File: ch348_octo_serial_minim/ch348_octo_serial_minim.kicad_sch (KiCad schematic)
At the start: 41 parts, among them J1 USB_C_Receptacle_USB2.0, J10 JLCPCB_3.5MM_SOCKET_C18166, J12 JLCPCB_3.5MM_SOCKET_C18166, J14 JLCPCB_3.5MM_SOCKET_C18166, J16 JLCPCB_3.5MM_SOCKET_C18166, J18 JLCPCB_3.5MM_SOCKET_C18166, J2 Conn_01x01, J20 JLCPCB_3.5MM_SOCKET_C18166, J3 Conn_01x01, J4 Conn_01x01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

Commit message: ch348_octo_serial_minim: jan2023 rev ready for production
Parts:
- removed R1, R9: 1k, tom-passives:R_0402_1005Metric, symbol jlcpcb-basic-resistor-0402:1k
- added J22, J23: Conn_01x16, tom-connectors:PinHeader_1x16_P2.54mm_Horizontal, symbol tom-connectors:Conn_01x16
- added R1: 2.4k, R_0402_1005Metric, symbol jlcpcb-basic-resistor-0402:2.4k
- added R9: 1.5k, R_0402_1005Metric, symbol jlcpcb-basic-resistor-0402:1.5k
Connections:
- net +3.3V: now also J22.10 (Pin_10), J22.14 (Pin_14), J22.2 (Pin_2), J22.6 (Pin_6), J23.10 (Pin_10), J23.14 (Pin_14), J23.2 (Pin_2), J23.6 (Pin_6), R1.1
- net GND: now also J22.1 (Pin_1), J22.13 (Pin_13), J22.5 (Pin_5), J22.9 (Pin_9), J23.1 (Pin_1), J23.13 (Pin_13), J23.5 (Pin_5), J23.9 (Pin_9)
- net RXD0: now also J22.4 (Pin_4)
- net RXD1: now also J22.8 (Pin_8)
- net RXD2: now also J22.12 (Pin_12)
- net RXD3: now also J22.16 (Pin_16)
- net RXD4: now also J23.4 (Pin_4)
- net RXD5: now also J23.8 (Pin_8)
- net RXD6: now also J23.12 (Pin_12)
- net RXD7: now also J23.16 (Pin_16)
- net TXD0: now also J22.3 (Pin_3)
- net TXD1: now also J22.7 (Pin_7)
- net TXD2: now also J22.11 (Pin_11)
- net TXD3: now also J22.15 (Pin_15)
- net TXD4: now also J23.3 (Pin_3)
- net TXD5: now also J23.7 (Pin_7)
- net TXD6: now also J23.11 (Pin_11)
- net TXD7: now also J23.15 (Pin_15)
- net TX_S: now also R9.2
- net at D4.2 (A): now also R9.1
- net at D1.2 (A): now also R1.2
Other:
- sheet Serial Connector 0 ports: added none; removed CTS, DTR, RTS, RXD, TXD
- sheet Serial Connector 1 ports: added none; removed CTS, DTR, RTS, RXD, TXD
- sheet Serial Connector 2 ports: added none; removed CTS, DTR, RTS, RXD, TXD
- sheet Serial Connector 3 ports: added none; removed CTS, DTR, RTS, RXD, TXD
- sheet Serial Connector 4 ports: added none; removed CTS, DTR, RTS, RXD, TXD
- sheet Serial Connector 5 ports: added none; removed CTS, DTR, RTS, RXD, TXD
- sheet Serial Connector 6 ports: added none; removed CTS, DTR, RTS, RXD, TXD
- sheet Serial Connector 7 ports: added none; removed CTS, DTR, RTS, RXD, TXD
- note removed: "Update led resistors!"
- note removed: "horizontal with most stock C725908"
- moved on the sheet: C11, C7, C9

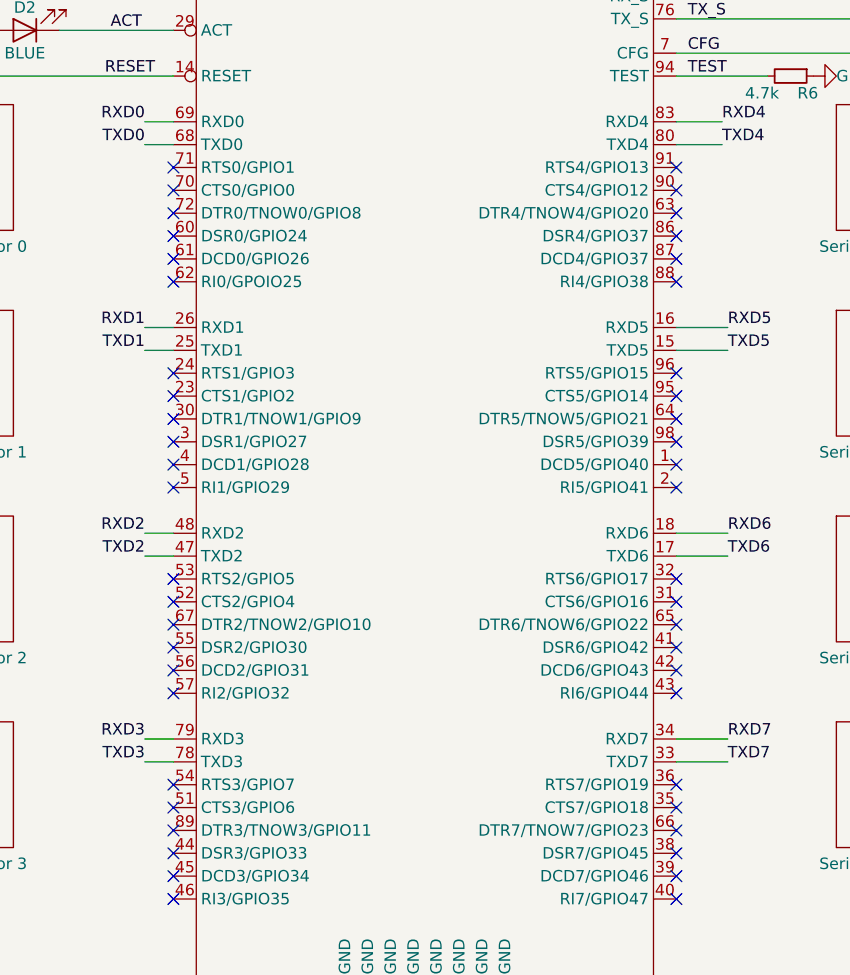
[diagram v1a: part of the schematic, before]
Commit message: ch348_octo_serial_minim: move plate to subdir, add cts/rts link, Jan2023a
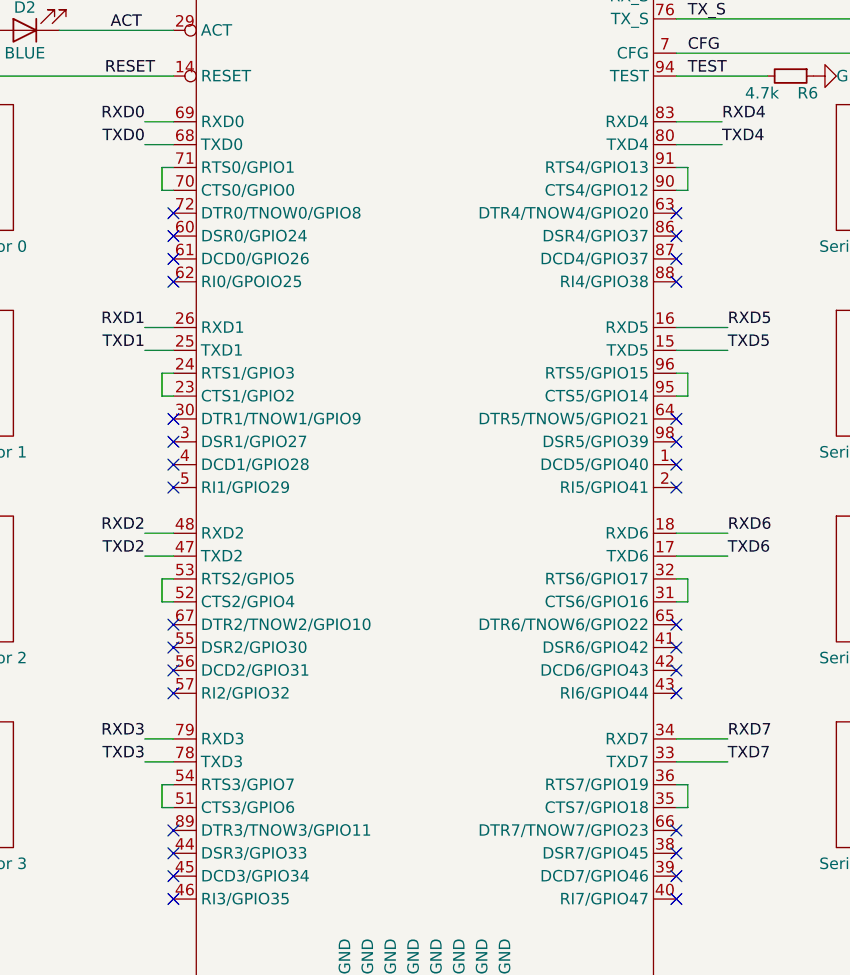
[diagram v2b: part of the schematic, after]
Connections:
- net at U1.23 (CTS1/GPIO2): now also U1.24 (RTS1/GPIO3)
- net at U1.31 (CTS6/GPIO16): now also U1.32 (RTS6/GPIO17)
- net at U1.35 (CTS7/GPIO18): now also U1.36 (RTS7/GPIO19)
- net at U1.51 (CTS3/GPIO6): now also U1.54 (RTS3/GPIO7)
- net at U1.52 (CTS2/GPIO4): now also U1.53 (RTS2/GPIO5)
- net at U1.70 (CTS0/GPIO0): now also U1.71 (RTS0/GPIO1)
- net at U1.90 (CTS4/GPIO12): now also U1.91 (RTS4/GPIO13)
- net at U1.95 (CTS5/GPIO14): now also U1.96 (RTS5/GPIO15)
- no-connect marks 54 -> 38
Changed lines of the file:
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@@
   (junction (at 58.42 81.915) (diameter 0) (color 0 0 0 0)
   )
-  (no_connect (at 165.735 83.82))
   (no_connect (at 109.855 132.08))
   (no_connect (at 109.855 71.12))
@@
   (no_connect (at 109.855 109.22))
   (no_connect (at 40.64 48.26))
-  (no_connect (at 109.855 58.42))
   (no_connect (at 165.735 137.16))
-  (no_connect (at 109.855 106.68))
   (no_connect (at 109.855 86.36))
   (no_connect (at 40.64 50.8))
-  (no_connect (at 165.735 104.14))
-  (no_connect (at 109.855 81.28))
-  (no_connect (at 109.855 60.96))
-  (no_connect (at 165.735 81.28))
   (no_connect (at 165.735 114.3))
   (no_connect (at 109.855 88.9))
   (no_connect (at 165.735 88.9))
-  (no_connect (at 165.735 129.54))
-  (no_connect (at 165.735 127))
-  (no_connect (at 165.735 106.68))
   (no_connect (at 165.735 71.12))
   (no_connect (at 182.88 172.085))
@@
   (no_connect (at 165.735 68.58))
   (no_connect (at 165.735 66.04))
-  (no_connect (at 109.855 127))
   (no_connect (at 109.855 63.5))
   (no_connect (at 165.735 111.76))
-  (no_connect (at 109.855 129.54))
   (no_connect (at 165.735 139.7))
   (no_connect (at 207.01 172.085))
   (no_connect (at 109.855 116.84))
-  (no_connect (at 109.855 104.14))
   (no_connect (at 109.855 114.3))
   (no_connect (at 109.855 91.44))
-  (no_connect (at 165.735 58.42))
-  (no_connect (at 165.735 60.96))
-  (no_connect (at 109.855 83.82))
   (wire (pts (xy 165.735 48.26) (xy 175.895 48.26))
     (stroke (width 0) (type default) (color 0 0 0 0))
@@
     (stroke (width 0) (type default) (color 0 0 0 0))
   )
+  (wire (pts (xy 108.585 60.96) (xy 109.855 60.96))
+    (stroke (width 0) (type default) (color 0 0 0 0))
+  )
   (wire (pts (xy 62.23 176.53) (xy 62.23 179.705))
     (stroke (width 0) (type default) (color 0 0 0 0))
@@
     (stroke (width 0) (type default) (color 0 0 0 0))
   )
+  (wire (pts (xy 108.585 104.14) (xy 108.585 106.68))
+    (stroke (width 0) (type default) (color 0 0 0 0))
+  )
   (wire (pts (xy 66.04 43.815) (xy 76.2 43.815))
     (stroke (width 0) (type default) (color 0 0 0 0))
@@
     (stroke (width 0) (type default) (color 0 0 0 0))
   )
+  (wire (pts (xy 165.735 58.42) (xy 167.005 58.42))
+    (stroke (width 0) (type default) (color 0 0 0 0))
+  )
+  (wire (pts (xy 109.855 127) (xy 108.585 127))
+    (stroke (width 0) (type default) (color 0 0 0 0))
+  )
   (wire (pts (xy 90.805 176.53) (xy 90.805 179.705))
     (stroke (width 0) (type default) (color 0 0 0 0))
@@
     (stroke (width 0) (type default) (color 0 0 0 0))
   )
+  (wire (pts (xy 165.735 127) (xy 167.005 127))
+    (stroke (width 0) (type default) (color 0 0 0 0))
+  )
   (wire (pts (xy 40.64 178.435) (xy 31.115 178.435))
     (stroke (width 0) (type default) (color 0 0 0 0))
@@
     (stroke (width 0) (type default) (color 0 0 0 0))
   )
+  (wire (pts (xy 108.585 106.68) (xy 109.855 106.68))
+    (stroke (width 0) (type default) (color 0 0 0 0))
+  )
   (wire (pts (xy 41.91 33.02) (xy 41.91 35.56))
     (stroke (width 0) (type default) (color 0 0 0 0))
@@
     (stroke (width 0) (type default) (color 0 0 0 0))
   )
+  (wire (pts (xy 109.855 81.28) (xy 108.585 81.28))
+    (stroke (width 0) (type default) (color 0 0 0 0))
+  )
   (wire (pts (xy 97.155 43.18) (xy 109.855 43.18))
     (stroke (width 0) (type default) (color 0 0 0 0))
@@
     (stroke (width 0) (type default) (color 0 0 0 0))
   )
+  (wire (pts (xy 167.005 104.14) (xy 167.005 106.68))
+    (stroke (width 0) (type default) (color 0 0 0 0))
+  )
   (wire (pts (xy 26.67 176.53) (xy 26.67 179.705))
     (stroke (width 0) (type default) (color 0 0 0 0))
@@
     (stroke (width 0) (type default) (color 0 0 0 0))
   )
+  (wire (pts (xy 165.735 106.68) (xy 167.005 106.68))
+    (stroke (width 0) (type default) (color 0 0 0 0))
+  )
   (wire (pts (xy 45.72 176.53) (xy 45.72 179.705))
     (stroke (width 0) (type default) (color 0 0 0 0))
@@
     (stroke (width 0) (type default) (color 0 0 0 0))
   )
+  (wire (pts (xy 108.585 83.82) (xy 109.855 83.82))
+    (stroke (width 0) (type default) (color 0 0 0 0))
+  )
   (wire (pts (xy 253.365 130.81) (xy 258.445 130.81))
     (stroke (width 0) (type default) (color 0 0 0 0))
@@
     (stroke (width 0) (type default) (color 0 0 0 0))
   )
+  (wire (pts (xy 165.735 129.54) (xy 167.005 129.54))
+    (stroke (width 0) (type default) (color 0 0 0 0))
+  )
   (wire (pts (xy 79.375 121.92) (xy 78.105 121.92))
     (stroke (width 0) (type default) (color 0 0 0 0))
@@
     (stroke (width 0) (type default) (color 0 0 0 0))
   )
+  (wire (pts (xy 108.585 81.28) (xy 108.585 83.82))
+    (stroke (width 0) (type default) (color 0 0 0 0))
+  )
   (wire (pts (xy 67.31 66.675) (xy 67.31 71.12))
     (stroke (width 0) (type default) (color 0 0 0 0))
@@
     (stroke (width 0) (type default) (color 0 0 0 0))
   )
+  (wire (pts (xy 165.735 60.96) (xy 167.005 60.96))
+    (stroke (width 0) (type default) (color 0 0 0 0))
+  )
   (wire (pts (xy 41.91 20.32) (xy 49.53 20.32))
     (stroke (width 0) (type default) (color 0 0 0 0))
@@
     (stroke (width 0) (type default) (color 0 0 0 0))
   )
+  (wire (pts (xy 108.585 129.54) (xy 109.855 129.54))
+    (stroke (width 0) (type default) (color 0 0 0 0))
+  )
   (wire (pts (xy 255.905 118.11) (xy 258.445 118.11))
     (stroke (width 0) (type default) (color 0 0 0 0))
@@
     (stroke (width 0) (type default) (color 0 0 0 0))
   )
+  (wire (pts (xy 165.735 83.82) (xy 167.005 83.82))
+    (stroke (width 0) (type default) (color 0 0 0 0))
+  )
   (wire (pts (xy 31.115 178.435) (xy 21.59 178.435))
     (stroke (width 0) (type default) (color 0 0 0 0))
@@
     (stroke (width 0) (type default) (color 0 0 0 0))
   )
+  (wire (pts (xy 167.005 81.28) (xy 167.005 83.82))
+    (stroke (width 0) (type default) (color 0 0 0 0))
+  )
   (wire (pts (xy 165.735 55.88) (xy 170.815 55.88))
     (stroke (width 0) (type default) (color 0 0 0 0))
@@
     (stroke (width 0) (type default) (color 0 0 0 0))
   )
+  (wire (pts (xy 108.585 58.42) (xy 108.585 60.96))
+    (stroke (width 0) (type default) (color 0 0 0 0))
+  )
   (wire (pts (xy 41.91 38.1) (xy 109.855 38.1))
     (stroke (width 0) (type default) (color 0 0 0 0))
   )
+  (wire (pts (xy 165.735 81.28) (xy 167.005 81.28))
+    (stroke (width 0) (type default) (color 0 0 0 0))
+  )
   (wire (pts (xy 49.53 76.2) (xy 49.53 81.915))
     (stroke (width 0) (type default) (color 0 0 0 0))
@@
     (stroke (width 0) (type default) (color 0 0 0 0))
   )
+  (wire (pts (xy 109.855 104.14) (xy 108.585 104.14))
+    (stroke (width 0) (type default) (color 0 0 0 0))
+  )
+  (wire (pts (xy 109.855 58.42) (xy 108.585 58.42))
+    (stroke (width 0) (type default) (color 0 0 0 0))
+  )
   (wire (pts (xy 144.145 152.4) (xy 146.685 152.4))
     (stroke (width 0) (type default) (color 0 0 0 0))
@@
     (stroke (width 0) (type default) (color 0 0 0 0))
   )
+  (wire (pts (xy 165.735 104.14) (xy 167.005 104.14))
+    (stroke (width 0) (type default) (color 0 0 0 0))
+  )
   (wire (pts (xy 253.365 95.885) (xy 258.445 95.885))
     (stroke (width 0) (type default) (color 0 0 0 0))
@@
     (stroke (width 0) (type default) (color 0 0 0 0))
   )
+  (wire (pts (xy 167.005 127) (xy 167.005 129.54))
+    (stroke (width 0) (type default) (color 0 0 0 0))
+  )
   (wire (pts (xy 189.865 20.955) (xy 189.865 22.86))
     (stroke (width 0) (type default) (color 0 0 0 0))
   )
+  (wire (pts (xy 167.005 58.42) (xy 167.005 60.96))
+    (stroke (width 0) (type default) (color 0 0 0 0))
+  )
   (wire (pts (xy 257.175 23.495) (xy 266.065 23.495))
     (stroke (width 0) (type default) (color 0 0 0 0))
@@
     (stroke (width 0) (type default) (color 0 0 0 0))
   )
+  (wire (pts (xy 108.585 127) (xy 108.585 129.54))
+    (stroke (width 0) (type default) (color 0 0 0 0))
+  )
